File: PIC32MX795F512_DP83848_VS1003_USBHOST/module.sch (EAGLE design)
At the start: 116 parts, among them IC1 IC_USBLC6-2, IC2 LM1117IMPX-3.3, IC3 PIC32MX795F512, IC4 DP83848, IC5 LM1117MPX-2.5, U1 USD-SOCKETUSD, U2 VS1003, X2 CRYSTALS-NOGND-CFPX-217, X3 KUSBVX, Y1 CRYSTAL-GROUNDEDSMD-5X3.2, Y3 CRYSTAL-GROUNDEDSMD-5X3.2

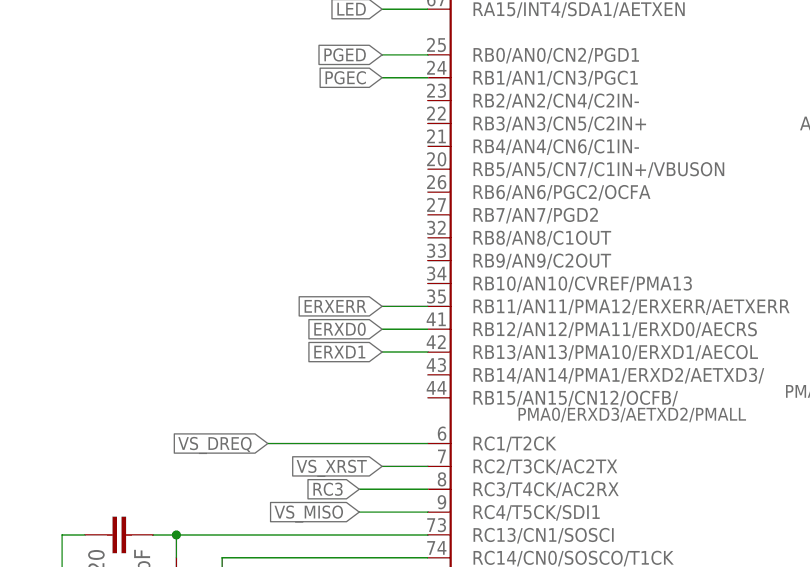
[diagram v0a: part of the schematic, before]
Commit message: DP83848 RST line added
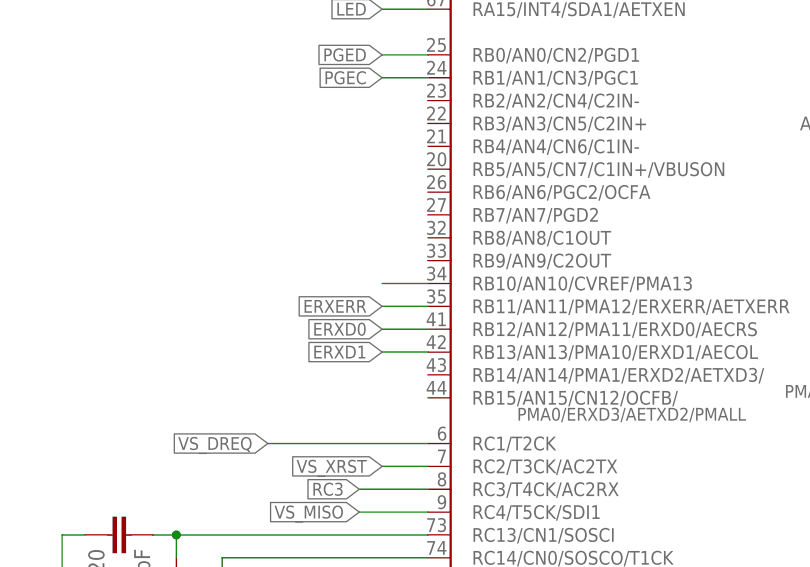
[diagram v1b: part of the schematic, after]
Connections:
- removed net N$2: IC4.RESET_N, R1.2
- new net DP_RST: IC3.RB10/AN10/CVREF/PMA13, IC4.RESET_N, R1.2
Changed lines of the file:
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@@
 </segment>
 </net>
-<net name="N$2" class="0">
+<net name="DP_RST" class="0">
 <segment>
 <pinref part="R1" gate="G$1" pin="2"/>
@@
 <wire x1="391.16" y1="-68.58" x2="391.16" y2="-91.44" width="0.1524" layer="91"/>
 </segment>
+<segment>
+<pinref part="IC3" gate="G$1" pin="RB10/AN10/CVREF/PMA13"/>
+<wire x1="20.32" y1="375.92" x2="15.24" y2="375.92" width="0.1524" layer="91"/>
+</segment>
 </net>

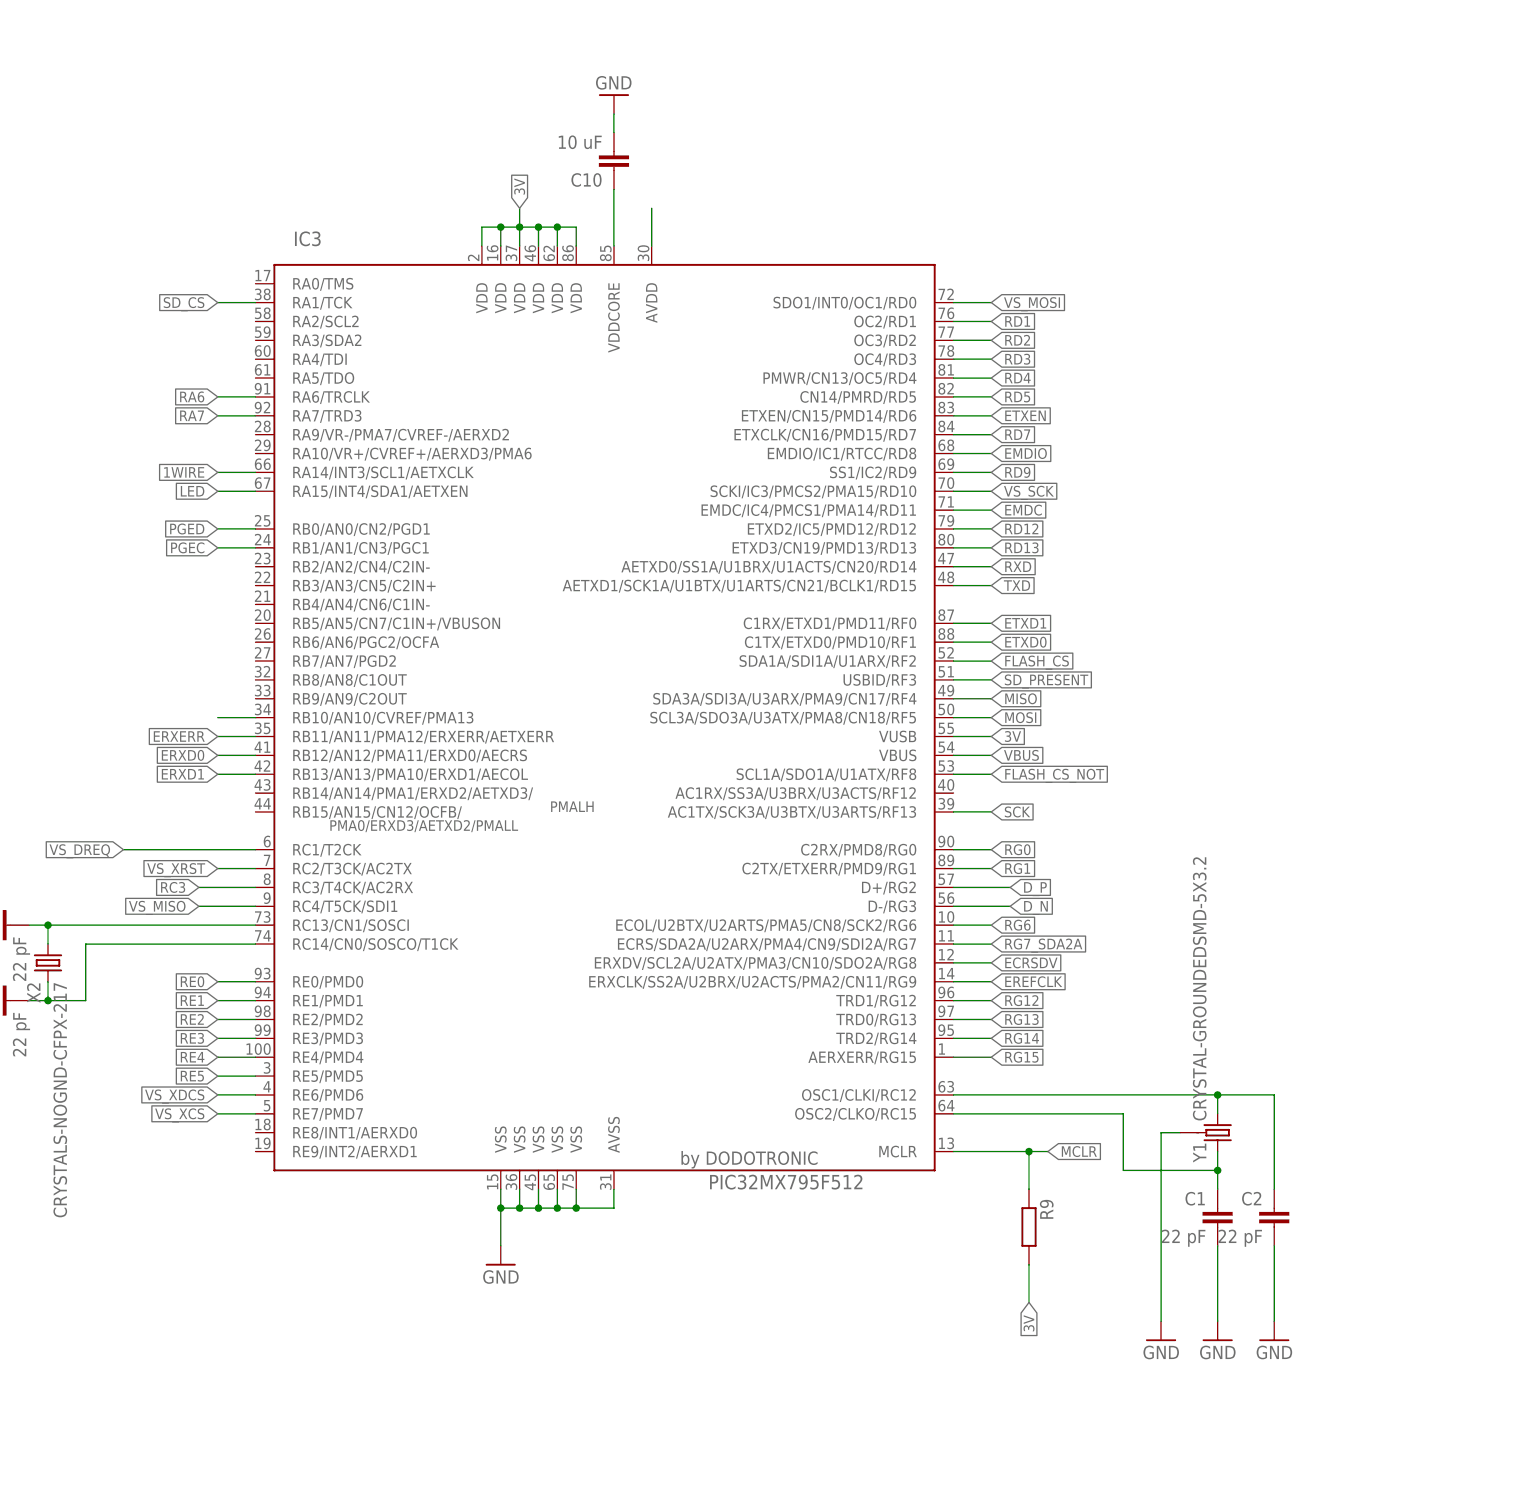
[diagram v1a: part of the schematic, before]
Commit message: Crystl generator added
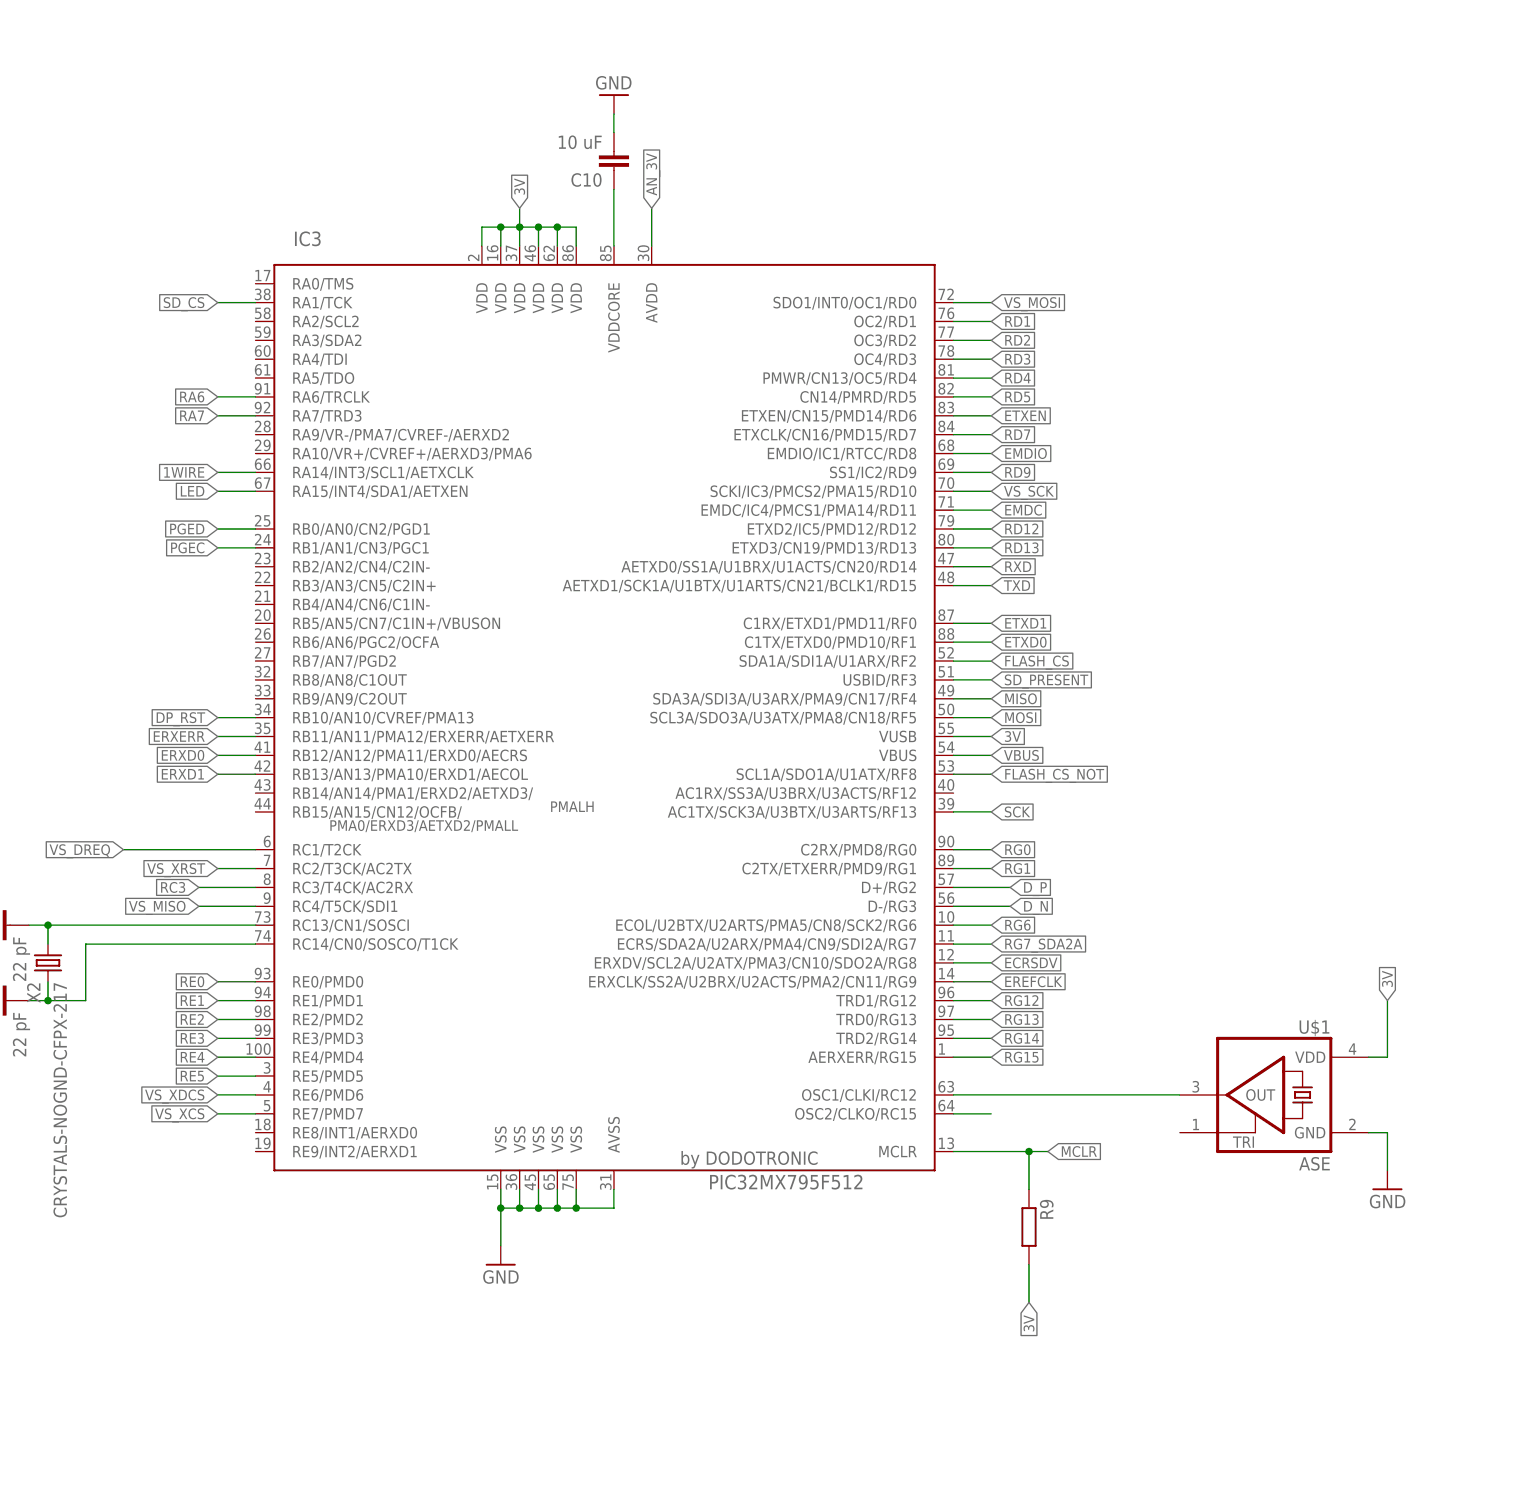
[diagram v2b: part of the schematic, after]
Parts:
- removed C1, C2: 22 pF, rcl:C-EUC0603
- removed Y1: CRYSTAL-GROUNDEDSMD-5X3.2, SparkFun-Clocks:CRYSTAL-GROUNDEDSMD-5X3.2
- added U$1: ASE, crystal:ASE
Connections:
- removed net OSC1: C2.1, IC3.OSC1/CLKI/RC12, Y1.2
- removed net OSC2: C1.1, IC3.OSC2/CLKO/RC15, Y1.1
- new net PH0: IC3.OSC1/CLKI/RC12, U$1.OUT
- new net RC15: IC3.OSC2/CLKO/RC15
- net 3V: now also U$1.VDD
- net GND: now also U$1.GND; no longer C1.2, C2.2, Y1.3
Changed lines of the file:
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@@
 <part name="C10" library="rcl" deviceset="C-EU" device="C0603" value="10 uF"/>
 <part name="GND18" library="SparkFun-Aesthetics" deviceset="GND" device=""/>
-<part name="C1" library="rcl" deviceset="C-EU" device="C0603" value="22 pF"/>
-<part name="C2" library="rcl" deviceset="C-EU" device="C0603" value="22 pF"/>
-<part name="GND3" library="supply1" deviceset="GND" device=""/>
-<part name="GND35" library="supply1" deviceset="GND" device=""/>
-<part name="Y1" library="SparkFun-Clocks" deviceset="CRYSTAL-GROUNDED" device="SMD-5X3.2"/>
-<part name="GND1" library="supply1" deviceset="GND" device=""/>
 <part name="IC1" library="dp_devices" deviceset="IC_USBLC6-2" device=""/>
 <part name="GND31" library="supply1" deviceset="GND" device=""/>
@@
 <part name="GND55" library="supply1" deviceset="GND" device=""/>
 <part name="GND73" library="supply1" deviceset="GND" device=""/>
+<part name="U$1" library="crystal" deviceset="ASE" device=""/>
+<part name="GND74" library="supply1" deviceset="GND" device=""/>
 </parts>
 <sheets>
@@
 <instance part="C10" gate="G$1" x="68.58" y="449.58" rot="R180"/>
 <instance part="GND18" gate="1" x="68.58" y="459.74" rot="MR180"/>
-<instance part="C1" gate="G$1" x="149.86" y="309.88" rot="MR0"/>
-<instance part="C2" gate="G$1" x="157.48" y="309.88" rot="MR0"/>
-<instance part="GND3" gate="1" x="149.86" y="292.1" rot="MR0"/>
-<instance part="GND35" gate="1" x="157.48" y="292.1" rot="MR0"/>
-<instance part="Y1" gate="G$1" x="149.86" y="320.04" rot="MR90"/>
-<instance part="GND1" gate="1" x="142.24" y="292.1" rot="MR0"/>
 <instance part="IC1" gate="G$1" x="322.58" y="363.22" rot="R180"/>
 <instance part="GND31" gate="1" x="347.98" y="320.04"/>
@@
 <instance part="GND55" gate="1" x="342.9" y="236.22"/>
 <instance part="GND73" gate="1" x="322.58" y="236.22"/>
+<instance part="U$1" gate="G$1" x="157.48" y="325.12" rot="MR0"/>
+<instance part="GND74" gate="1" x="172.72" y="312.42" rot="MR0"/>
 </instances>
 <busses>
@@
 <pinref part="GND18" gate="1" pin="GND"/>
 <wire x1="68.58" y1="457.2" x2="68.58" y2="454.66" width="0.1524" layer="91"/>
-</segment>
-<segment>
-<pinref part="C1" gate="G$1" pin="2"/>
-<pinref part="GND3" gate="1" pin="GND"/>
-<wire x1="149.86" y1="294.64" x2="149.86" y2="304.8" width="0.1524" layer="91"/>
-</segment>
-<segment>
-<pinref part="C2" gate="G$1" pin="2"/>
-<pinref part="GND35" gate="1" pin="GND"/>
-<wire x1="157.48" y1="294.64" x2="157.48" y2="304.8" width="0.1524" layer="91"/>
-</segment>
-<segment>
-<pinref part="Y1" gate="G$1" pin="3"/>
-<pinref part="GND1" gate="1" pin="GND"/>
-<wire x1="144.78" y1="320.04" x2="142.24" y2="320.04" width="0.1524" layer="91"/>
-<wire x1="142.24" y1="320.04" x2="142.24" y2="294.64" width="0.1524" layer="91"/>
 </segment>
 <segment>
@@
 <wire x1="325.12" y1="246.38" x2="322.58" y2="246.38" width="0.1524" layer="91"/>
 <junction x="322.58" y="246.38"/>
+</segment>
+<segment>
+<pinref part="U$1" gate="G$1" pin="GND"/>
+<pinref part="GND74" gate="1" pin="GND"/>
+<wire x1="170.18" y1="320.04" x2="172.72" y2="320.04" width="0.1524" layer="91"/>
+<wire x1="172.72" y1="320.04" x2="172.72" y2="314.96" width="0.1524" layer="91"/>
 </segment>
 </net>
@@
 <label x="403.86" y="-172.72" size="1.4224" layer="95" xref="yes"/>
 </segment>
+<segment>
+<pinref part="U$1" gate="G$1" pin="VDD"/>
+<wire x1="170.18" y1="330.2" x2="172.72" y2="330.2" width="0.1524" layer="91"/>
+<wire x1="172.72" y1="330.2" x2="172.72" y2="337.82" width="0.1524" layer="91"/>
+<label x="172.72" y="337.82" size="1.4224" layer="95" rot="MR90" xref="yes"/>
+</segment>
 </net>
 <net name="SOSCI" class="0">
@@
 <wire x1="68.58" y1="447.04" x2="68.58" y2="439.42" width="0.1524" layer="91"/>
 <pinref part="IC3" gate="G$1" pin="VDDCORE"/>
-</segment>
-</net>
-<net name="OSC2" class="0">
-<segment>
-<wire x1="149.86" y1="314.96" x2="149.86" y2="317.5" width="0.1524" layer="91"/>
-<pinref part="C1" gate="G$1" pin="1"/>
-<wire x1="149.86" y1="314.96" x2="149.86" y2="312.42" width="0.1524" layer="91"/>
-<junction x="149.86" y="314.96"/>
-<pinref part="Y1" gate="G$1" pin="1"/>
-<wire x1="114.3" y1="322.58" x2="137.16" y2="322.58" width="0.1524" layer="91"/>
-<wire x1="137.16" y1="322.58" x2="137.16" y2="314.96" width="0.1524" layer="91"/>
-<wire x1="137.16" y1="314.96" x2="149.86" y2="314.96" width="0.1524" layer="91"/>
-<pinref part="IC3" gate="G$1" pin="OSC2/CLKO/RC15"/>
-</segment>
-</net>
-<net name="OSC1" class="0">
-<segment>
-<wire x1="149.86" y1="325.12" x2="149.86" y2="322.58" width="0.1524" layer="91"/>
-<pinref part="C2" gate="G$1" pin="1"/>
-<wire x1="149.86" y1="325.12" x2="157.48" y2="325.12" width="0.1524" layer="91"/>
-<wire x1="157.48" y1="325.12" x2="157.48" y2="312.42" width="0.1524" layer="91"/>
-<junction x="149.86" y="325.12"/>
-<pinref part="Y1" gate="G$1" pin="2"/>
-<wire x1="114.3" y1="325.12" x2="149.86" y2="325.12" width="0.1524" layer="91"/>
-<pinref part="IC3" gate="G$1" pin="OSC1/CLKI/RC12"/>
 </segment>
 </net>
@@
 <pinref part="IC3" gate="G$1" pin="AVDD"/>
 <wire x1="73.66" y1="439.42" x2="73.66" y2="444.5" width="0.1524" layer="91"/>
+<label x="73.66" y="444.5" size="1.4224" layer="95" rot="R90" xref="yes"/>
 </segment>
 <segment>
@@
 <pinref part="IC3" gate="G$1" pin="RB10/AN10/CVREF/PMA13"/>
 <wire x1="20.32" y1="375.92" x2="15.24" y2="375.92" width="0.1524" layer="91"/>
-</segment>
-</net>
+<label x="15.24" y="375.92" size="1.4224" layer="95" rot="R180" xref="yes"/>
+</segment>
+</net>
+<net name="PH0" class="0">
+<segment>
+<pinref part="U$1" gate="G$1" pin="OUT"/>
+<pinref part="IC3" gate="G$1" pin="OSC1/CLKI/RC12"/>
+<wire x1="144.78" y1="325.12" x2="114.3" y2="325.12" width="0.1524" layer="91"/>
+</segment>
+</net>
+<net name="RC15" class="0">
+<segment>
+<pinref part="IC3" gate="G$1" pin="OSC2/CLKO/RC15"/>
+<wire x1="114.3" y1="322.58" x2="119.38" y2="322.58" width="0.1524" layer="91"/>
+</segment>
+</net>

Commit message: Minor changes
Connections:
- removed net FLASH_CS_NOT: IC3.SCL1A/SDO1A/U1ATX/RF8
- new net SCL1A: IC3.SCL1A/SDO1A/U1ATX/RF8, SV1.1
- net 1WIRE: now also SV1.3
- net GND: no longer SV1.3, SV1.4, SV1.5, SV1.6, SV1.8
- net LED: now also SV1.6; no longer SV1.2
- net RC15: now also SV1.4
- net RD9: now also SV1.5; no longer SV1.1
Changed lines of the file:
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@@
 <part name="R1" library="rcl" deviceset="R-EU_" device="R0402"/>
 <part name="GND55" library="supply1" deviceset="GND" device=""/>
-<part name="GND73" library="supply1" deviceset="GND" device=""/>
 <part name="U$1" library="crystal" deviceset="ASE" device=""/>
 <part name="GND74" library="supply1" deviceset="GND" device=""/>
@@
 <instance part="R1" gate="G$1" x="391.16" y="-63.5" rot="R270"/>
 <instance part="GND55" gate="1" x="342.9" y="236.22"/>
-<instance part="GND73" gate="1" x="322.58" y="236.22"/>
 <instance part="U$1" gate="G$1" x="157.48" y="325.12" rot="MR0"/>
 <instance part="GND74" gate="1" x="172.72" y="312.42" rot="MR0"/>
@@
 <pinref part="GND54" gate="1" pin="GND"/>
 <wire x1="487.68" y1="-68.58" x2="487.68" y2="-66.04" width="0.1524" layer="91"/>
-</segment>
-<segment>
-<pinref part="SV1" gate="G$1" pin="5"/>
-<pinref part="GND55" gate="1" pin="GND"/>
-<wire x1="340.36" y1="248.92" x2="342.9" y2="248.92" width="0.1524" layer="91"/>
-<wire x1="342.9" y1="248.92" x2="342.9" y2="246.38" width="0.1524" layer="91"/>
-<pinref part="SV1" gate="G$1" pin="3"/>
-<wire x1="342.9" y1="246.38" x2="342.9" y2="238.76" width="0.1524" layer="91"/>
-<wire x1="340.36" y1="246.38" x2="342.9" y2="246.38" width="0.1524" layer="91"/>
-<junction x="342.9" y="246.38"/>
-</segment>
-<segment>
-<pinref part="SV1" gate="G$1" pin="8"/>
-<pinref part="GND73" gate="1" pin="GND"/>
-<wire x1="325.12" y1="251.46" x2="322.58" y2="251.46" width="0.1524" layer="91"/>
-<wire x1="322.58" y1="251.46" x2="322.58" y2="248.92" width="0.1524" layer="91"/>
-<pinref part="SV1" gate="G$1" pin="6"/>
-<wire x1="322.58" y1="248.92" x2="322.58" y2="246.38" width="0.1524" layer="91"/>
-<wire x1="322.58" y1="246.38" x2="322.58" y2="238.76" width="0.1524" layer="91"/>
-<wire x1="325.12" y1="248.92" x2="322.58" y2="248.92" width="0.1524" layer="91"/>
-<junction x="322.58" y="248.92"/>
-<pinref part="SV1" gate="G$1" pin="4"/>
-<wire x1="325.12" y1="246.38" x2="322.58" y2="246.38" width="0.1524" layer="91"/>
-<junction x="322.58" y="246.38"/>
 </segment>
 <segment>
@@
 </segment>
 <segment>
-<pinref part="SV1" gate="G$1" pin="1"/>
-<wire x1="340.36" y1="243.84" x2="345.44" y2="243.84" width="0.1524" layer="91"/>
-<label x="345.44" y="243.84" size="1.4224" layer="95" xref="yes"/>
+<pinref part="SV1" gate="G$1" pin="5"/>
+<wire x1="340.36" y1="248.92" x2="345.44" y2="248.92" width="0.1524" layer="91"/>
+<label x="345.44" y="248.92" size="1.4224" layer="95" xref="yes"/>
 </segment>
 </net>
@@
 <label x="15.24" y="408.94" size="1.4224" layer="95" rot="R180" xref="yes"/>
 </segment>
+<segment>
+<pinref part="SV1" gate="G$1" pin="3"/>
+<wire x1="340.36" y1="246.38" x2="345.44" y2="246.38" width="0.1524" layer="91"/>
+<label x="345.44" y="246.38" size="1.4224" layer="95" xref="yes"/>
+</segment>
 </net>
 <net name="LED" class="0">
@@
 </segment>
 <segment>
-<pinref part="SV1" gate="G$1" pin="2"/>
-<wire x1="325.12" y1="243.84" x2="320.04" y2="243.84" width="0.1524" layer="91"/>
-<label x="320.04" y="243.84" size="1.4224" layer="95" rot="R180" xref="yes"/>
+<pinref part="SV1" gate="G$1" pin="6"/>
+<wire x1="325.12" y1="248.92" x2="320.04" y2="248.92" width="0.1524" layer="91"/>
+<label x="320.04" y="248.92" size="1.4224" layer="95" rot="R180" xref="yes"/>
 </segment>
 </net>
@@
 </segment>
 </net>
-<net name="FLASH_CS_NOT" class="0">
+<net name="SCL1A" class="0">
 <segment>
 <pinref part="IC3" gate="G$1" pin="SCL1A/SDO1A/U1ATX/RF8"/>
@@
 <label x="119.38" y="368.3" size="1.4224" layer="95" xref="yes"/>
 </segment>
+<segment>
+<pinref part="SV1" gate="G$1" pin="1"/>
+<wire x1="340.36" y1="243.84" x2="345.44" y2="243.84" width="0.1524" layer="91"/>
+</segment>
 </net>
 <net name="DP_RST" class="0">
@@
 <wire x1="114.3" y1="322.58" x2="119.38" y2="322.58" width="0.1524" layer="91"/>
 </segment>
-</net>
+<segment>
+<pinref part="SV1" gate="G$1" pin="4"/>
+<wire x1="325.12" y1="246.38" x2="320.04" y2="246.38" width="0.1524" layer="91"/>
+<label x="320.04" y="246.38" size="1.4224" layer="95" rot="R180" xref="yes"/>
+</segment>
+</net>
